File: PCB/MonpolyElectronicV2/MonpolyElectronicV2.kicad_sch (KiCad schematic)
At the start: 2 parts

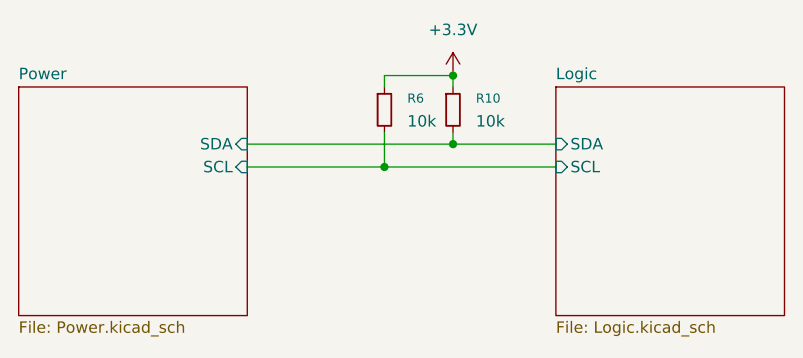
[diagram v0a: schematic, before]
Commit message: work on Logic part (MCU): audio done, programming done, ESP32 and inputs WIP, diplay not yet started
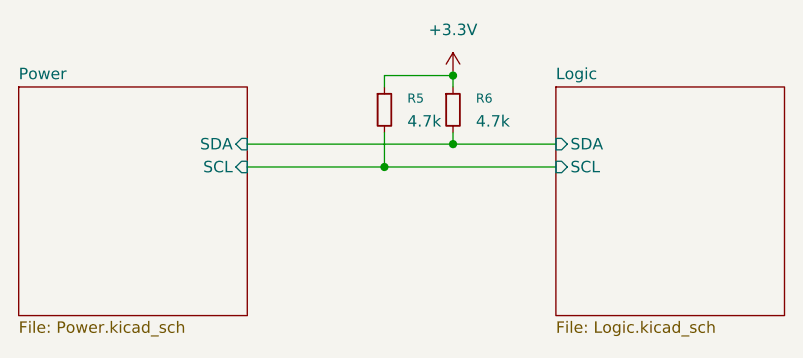
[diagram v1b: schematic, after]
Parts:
- removed R10: 10k, symbol Device:R_Small
- added R5: 4.7k, symbol Device:R_Small
- R6: value 10k -> 4.7k
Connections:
- net +3.3V: now also R5.1
- net Logic/SCL: now also R5.2; no longer R6.2
- net Logic/SDA: now also R6.2
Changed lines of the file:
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@@
+	(symbol
+		(lib_id "Device:R_Small")
+		(at 140.97 91.44 0)
+		(unit 1)
+		(exclude_from_sim no)
+		(in_bom yes)
+		(on_board yes)
+		(dnp no)
+		(fields_autoplaced yes)
+		(property "Reference" "R5"
+			(at 143.51 90.1699 0)
+			(effects
+				(font
+					(size 1.016 1.016)
+				)
+				(justify left)
+			)
+		)
+		(property "Value" "4.7k"
+			(at 143.51 92.7099 0)
+			(effects
+				(font
+					(size 1.27 1.27)
+				)
+				(justify left)
+			)
+		)
+		(property "Footprint" ""
+			(at 140.97 91.44 0)
+			(effects
+				(font
+					(size 1.27 1.27)
+				)
+				(hide yes)
+			)
+		)
+		(property "Datasheet" "~"
+			(at 140.97 91.44 0)
+			(effects
+				(font
+					(size 1.27 1.27)
+				)
+				(hide yes)
+			)
+		)
+		(property "Description" "Resistor, small symbol"
+			(at 140.97 91.44 0)
+			(effects
+				(font
+					(size 1.27 1.27)
+				)
+				(hide yes)
+			)
+		)
+		(pin "1"
+		)
+		(pin "2"
+		)
+		(instances
+			(project "MonpolyElectronicV2"
+				(path "/d7c31a86-0f1d-461f-96b3-0b094256e729"
+					(reference "R5")
+					(unit 1)
+				)
+			)
+		)
+	)
 	(symbol
 		(lib_id "Device:R_Small")
@@
 		(dnp no)
 		(fields_autoplaced yes)
-		(property "Reference" "R10"
+		(property "Reference" "R6"
 			(at 151.13 90.1699 0)
 			(effects
@@
 			)
 		)
-		(property "Value" "10k"
+		(property "Value" "4.7k"
 			(at 151.13 92.7099 0)
 			(effects
@@
 			(project "MonpolyElectronicV2"
 				(path "/d7c31a86-0f1d-461f-96b3-0b094256e729"
-					(reference "R10")
+					(reference "R6")
 					(unit 1)
 				)
@@
 					(unit 1)
 				)
-			)
-		)
-	)
-	(symbol
-		(lib_id "Device:R_Small")
-		(at 140.97 91.44 0)
-		(unit 1)
-		(exclude_from_sim no)
-		(in_bom yes)
-		(on_board yes)
-		(dnp no)
-		(fields_autoplaced yes)
-		(property "Reference" "R6"
-			(at 143.51 90.1699 0)
-			(effects
-				(font
-					(size 1.016 1.016)
-				)
-				(justify left)
-			)
-		)
-		(property "Value" "10k"
-			(at 143.51 92.7099 0)
-			(effects
-				(font
-					(size 1.27 1.27)
-				)
-				(justify left)
-			)
-		)
-		(property "Footprint" ""
-			(at 140.97 91.44 0)
-			(effects
-				(font
-					(size 1.27 1.27)
-				)
-				(hide yes)
-			)
-		)
-		(property "Datasheet" "~"
-			(at 140.97 91.44 0)
-			(effects
-				(font
-					(size 1.27 1.27)
-				)
-				(hide yes)
-			)
-		)
-		(property "Description" "Resistor, small symbol"
-			(at 140.97 91.44 0)
-			(effects
-				(font
-					(size 1.27 1.27)
-				)
-				(hide yes)
-			)
-		)
-		(pin "1"
-		)
-		(pin "2"
-		)
-		(instances
-			(project "MonpolyElectronicV2"
-				(path "/d7c31a86-0f1d-461f-96b3-0b094256e729"
-					(reference "R6")
-					(unit 1)
-				)

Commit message: add symbols + multiple backlight options
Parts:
- R5, R6: footprint (none) -> Resistor_SMD:R_0603_1608Metric
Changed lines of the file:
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@@
 			)
 		)
-		(property "Footprint" ""
+		(property "Footprint" "Resistor_SMD:R_0603_1608Metric"
 			(at 140.97 91.44 0)
 			(effects
@@
 			)
 		)
-		(property "Footprint" ""
+		(property "Footprint" "Resistor_SMD:R_0603_1608Metric"
 			(at 148.59 91.44 0)
 			(effects

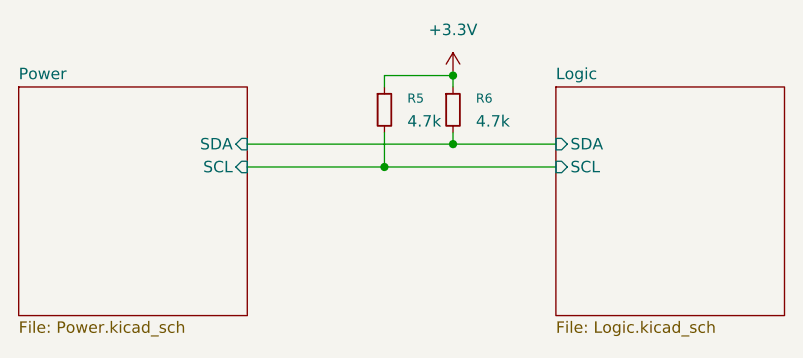
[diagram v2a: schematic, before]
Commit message: Start component placing by groups: BQ25895RTWR, TPS62162DSG and 10155435-00011LF done
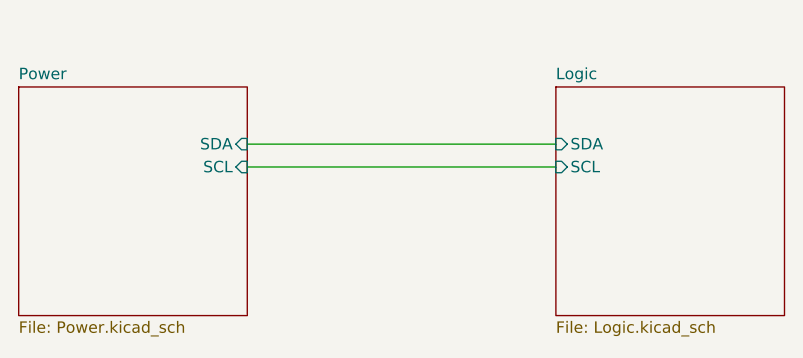
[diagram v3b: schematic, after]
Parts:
- removed R5, R6: 4.7k, Resistor_SMD:R_0603_1608Metric, symbol Device:R_Small
